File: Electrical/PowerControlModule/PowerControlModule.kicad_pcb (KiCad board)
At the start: 4 copper layers, 47 parts, among them J1 178.6164.0002, J10 Screw_Terminal_01x02, J11 Screw_Terminal_01x02, J12 Screw_Terminal_01x02, J13 Screw_Terminal_01x02, J14 Screw_Terminal_01x02, J15 Screw_Terminal_01x02, J16 Screw_Terminal_01x02, J17 Conn_01x03, J2 178.6164.0002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

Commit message: Fixes silkscreen stuff and adds ground connection for motor control battery connection
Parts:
- renumbered J17 to PowerConnection1
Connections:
- CONN10 pad 2: Net-(CONN10-Pad2) -> GND
- CONN11 pad 2: Net-(CONN11-Pad2) -> GND
- CONN12 pad 2: Net-(CONN11-Pad2) -> GND
- CONN9 pad 2: Net-(CONN10-Pad2) -> GND
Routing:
- net GND: track 0.00 -> 56.8 mm
- net Net-(CONN11-Pad2): track 28.9 -> 0.00 mm
- net Net-(CONN10-Pad2): track 27.9 -> 0.00 mm
- net +12V: track 6.88 -> 0.00 mm
- added copper zone on In1.Cu, net +12V
- added copper zone on In2.Cu, net GND
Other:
- net class Power: clearance 1 -> 0.5
- board text added: "+"
- board text added: "-"
- board text added: "12V"
- board text added: "ENABLE"
- board text added: "GND"

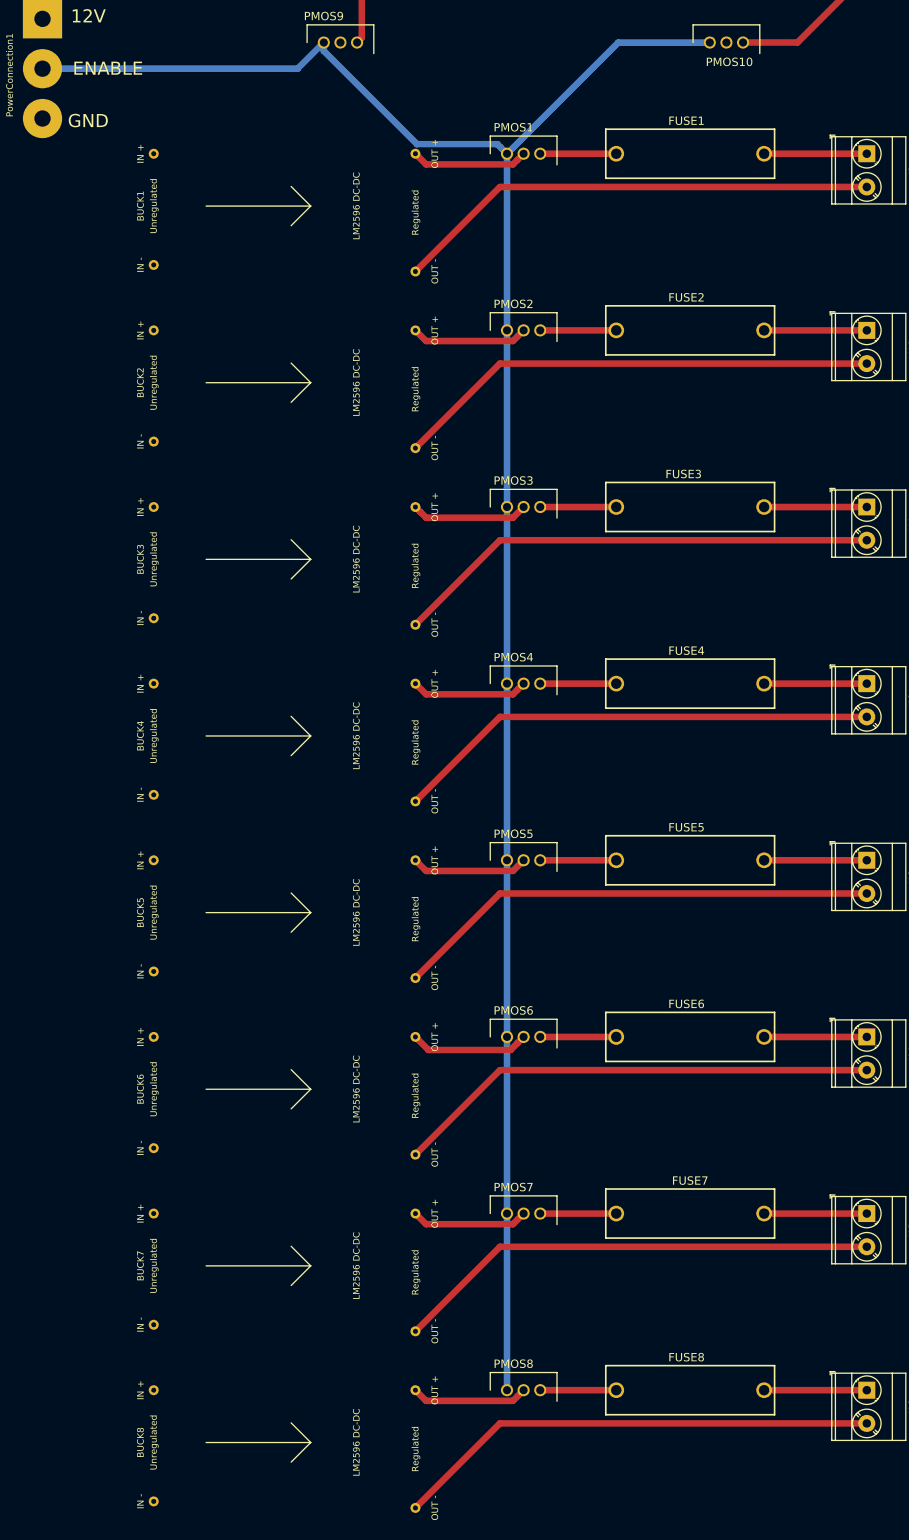
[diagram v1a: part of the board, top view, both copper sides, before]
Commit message: Rearranges mosfets, fuses and buck converters in correct order. Need to add heatsinks to design and confirm hole sizes. Also need to add safety module eventually
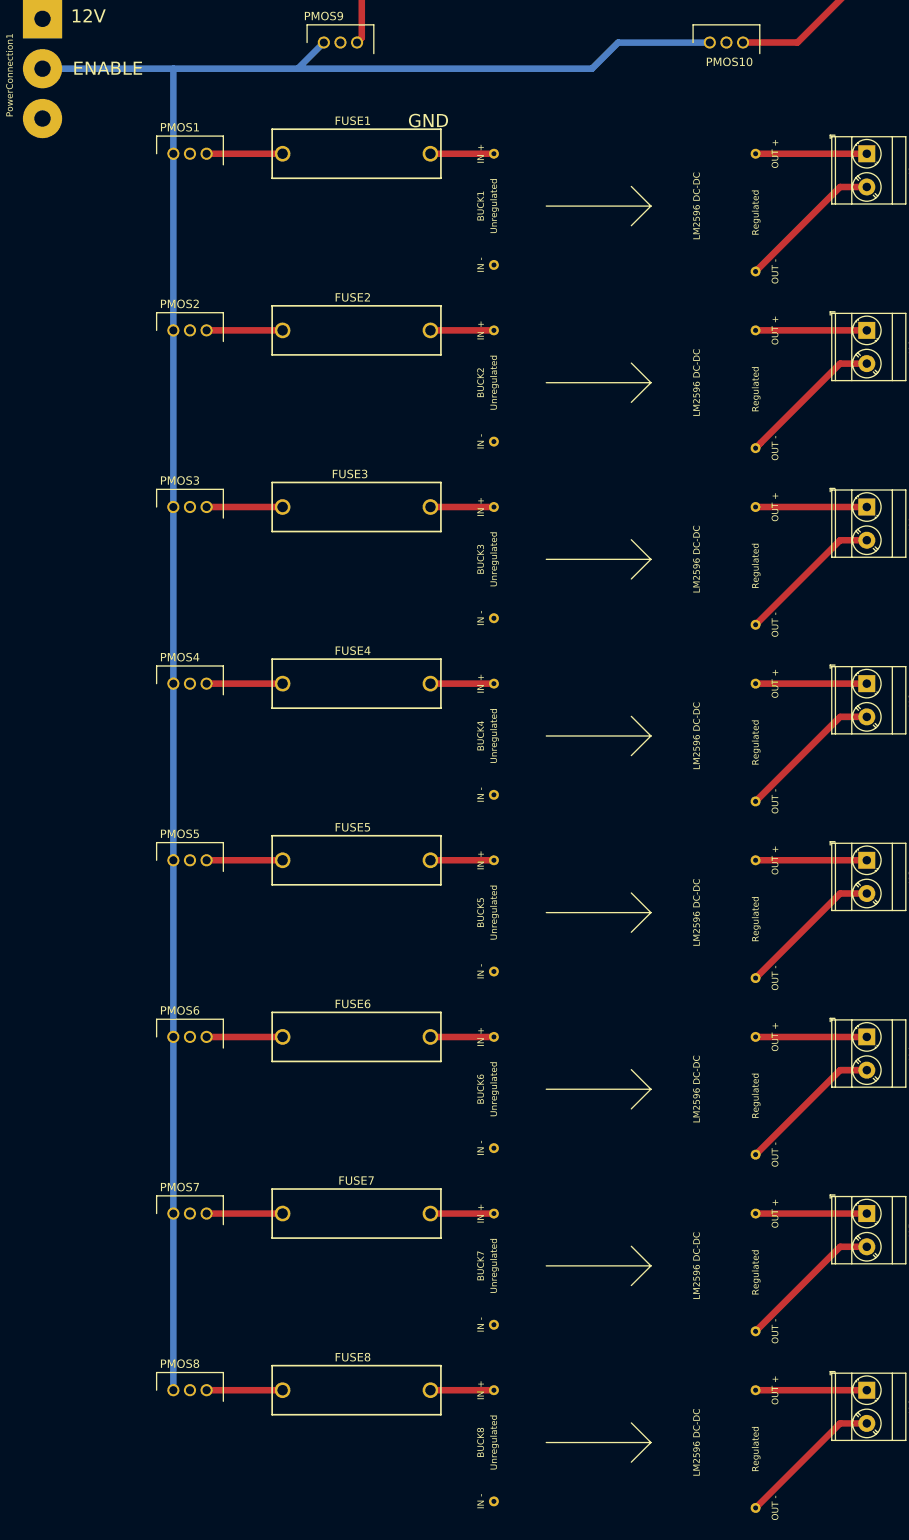
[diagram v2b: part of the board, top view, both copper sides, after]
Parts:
- moved BUCK1 52.0 mm to (368.0, 43.0)
- moved BUCK2 52.0 mm to (368.0, 70.0)
- moved BUCK3 52.0 mm to (368.0, 97.0)
- moved BUCK4 52.0 mm to (368.0, 124.0)
- moved BUCK5 52.0 mm to (368.0, 151.0)
- moved BUCK6 52.0 mm to (368.0, 178.0)
- moved BUCK7 52.0 mm to (368.0, 205.0)
- moved BUCK8 52.0 mm to (368.0, 232.0)
- moved FUSE1 51.0 mm to (350.0, 36.0)
- moved FUSE2 51.0 mm to (350.0, 63.0)
- moved FUSE3 51.0 mm to (350.0, 90.0)
- moved FUSE4 51.0 mm to (350.0, 117.0)
- moved FUSE5 51.0 mm to (350.0, 144.0)
- moved FUSE6 51.0 mm to (350.0, 171.0)
- moved FUSE7 51.0 mm to (350.0, 198.0)
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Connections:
- BUCK1 pad 2: +12V -> Net-(BUCK1-Pad2)
- BUCK2 pad 2: +12V -> Net-(BUCK2-Pad2)
- BUCK3 pad 2: +12V -> Net-(BUCK3-Pad2)
- BUCK4 pad 2: +12V -> Net-(BUCK4-Pad2)
- BUCK5 pad 2: +12V -> Net-(BUCK5-Pad2)
- BUCK6 pad 2: +12V -> Net-(BUCK6-Pad2)
- BUCK7 pad 2: +12V -> Net-(BUCK7-Pad2)
- BUCK8 pad 2: +12V -> Net-(BUCK8-Pad2)
- FUSE1 pad 2: Net-(FUSE1-Pad2) -> Net-(BUCK1-Pad2)
- FUSE2 pad 2: Net-(FUSE2-Pad2) -> Net-(BUCK2-Pad2)
- FUSE3 pad 2: Net-(FUSE3-Pad2) -> Net-(BUCK3-Pad2)
- FUSE4 pad 2: Net-(FUSE4-Pad2) -> Net-(BUCK4-Pad2)
- FUSE5 pad 2: Net-(FUSE5-Pad2) -> Net-(BUCK5-Pad2)
- FUSE6 pad 2: Net-(FUSE6-Pad2) -> Net-(BUCK6-Pad2)
- FUSE7 pad 2: Net-(FUSE7-Pad2) -> Net-(BUCK7-Pad2)
- FUSE8 pad 2: Net-(FUSE8-Pad2) -> Net-(BUCK8-Pad2)
- J10 pad 1: Net-(FUSE2-Pad2) -> Net-(BUCK2-Pad4)
- J11 pad 1: Net-(FUSE3-Pad2) -> Net-(BUCK3-Pad4)
- J12 pad 1: Net-(FUSE4-Pad2) -> Net-(BUCK4-Pad4)
- J13 pad 1: Net-(FUSE5-Pad2) -> Net-(BUCK5-Pad4)
- J14 pad 1: Net-(FUSE6-Pad2) -> Net-(BUCK6-Pad4)
- J15 pad 1: Net-(FUSE7-Pad2) -> Net-(BUCK7-Pad4)
- J16 pad 1: Net-(FUSE8-Pad2) -> Net-(BUCK8-Pad4)
- J9 pad 1: Net-(FUSE1-Pad2) -> Net-(BUCK1-Pad4)
- PMOS1 pad 2: Net-(BUCK1-Pad4) -> +12V
- PMOS2 pad 2: Net-(BUCK2-Pad4) -> +12V
- PMOS3 pad 2: Net-(BUCK3-Pad4) -> +12V
- PMOS4 pad 2: Net-(BUCK4-Pad4) -> +12V
- PMOS5 pad 2: Net-(BUCK5-Pad4) -> +12V
- PMOS6 pad 2: Net-(BUCK6-Pad4) -> +12V
- PMOS7 pad 2: Net-(BUCK7-Pad4) -> +12V
- PMOS8 pad 2: Net-(BUCK8-Pad4) -> +12V
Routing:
- net Net-(BUCK4-Pad3): track 74.4 -> 22.4 mm
- net Net-(BUCK3-Pad3): track 74.4 -> 22.4 mm
- net Net-(BUCK2-Pad3): track 74.4 -> 22.4 mm
- net Net-(BUCK1-Pad3): track 74.4 -> 22.4 mm
- net Net-(BUCK8-Pad3): track 74.4 -> 22.4 mm
- net Net-(BUCK7-Pad3): track 74.4 -> 22.4 mm
- net Net-(BUCK6-Pad3): track 74.4 -> 22.4 mm
- net Net-(BUCK5-Pad3): track 74.4 -> 22.4 mm
- net Net-(FUSE8-Pad2): track 15.7 -> 0.00 mm
- net Net-(FUSE7-Pad2): track 15.7 -> 0.00 mm
- net Net-(FUSE6-Pad2): track 15.7 -> 0.00 mm
- net Net-(FUSE5-Pad2): track 15.7 -> 0.00 mm
- net Net-(FUSE4-Pad2): track 15.7 -> 0.00 mm
- net Net-(FUSE3-Pad2): track 15.7 -> 0.00 mm
- net Net-(FUSE2-Pad2): track 15.7 -> 0.00 mm
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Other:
- net class Power: clearance 0.5 -> 0.25

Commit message: Peripheral changes and rewired PCB
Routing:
- net GND: track 56.8 -> 0.00 mm
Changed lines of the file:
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@@
     (thickness 1.6)
     (drawings 27)
-    (tracks 86)
+    (tracks 84)
     (zones 0)
     (modules 47)
@@
   (layers
     (0 F.Cu signal)
-    (1 In1.Cu power)
+    (1 In1.Cu power hide)
     (2 In2.Cu power)
     (31 B.Cu signal)
@@
   (segment (start 423.92 41.08) (end 411 54) (width 1) (layer F.Cu) (net 17))
   (segment (start 428 41.08) (end 423.92 41.08) (width 1) (layer F.Cu) (net 17))
-  (segment (start 329 -21) (end 356.92 -21) (width 1) (layer F.Cu) (net 18))
-  (segment (start 425 -21) (end 396.08 -21) (width 1) (layer F.Cu) (net 18))
   (segment (start 428 63) (end 411 63) (width 1) (layer F.Cu) (net 19))
   (segment (start 411.761999 80.238001) (end 411 81) (width 1) (layer F.Cu) (net 20))

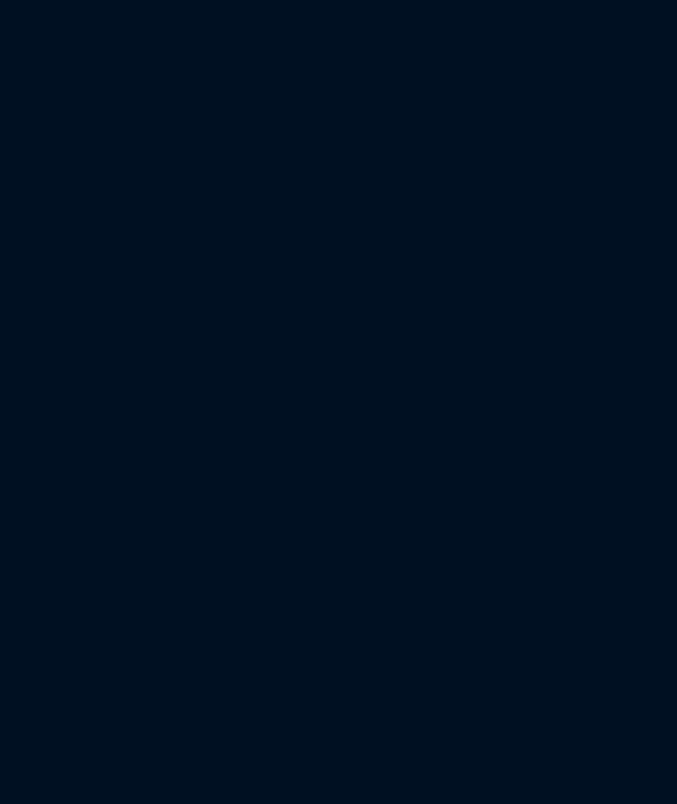
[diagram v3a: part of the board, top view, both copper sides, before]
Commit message: Splits project into multiple modules, peripherals, motors, and safety
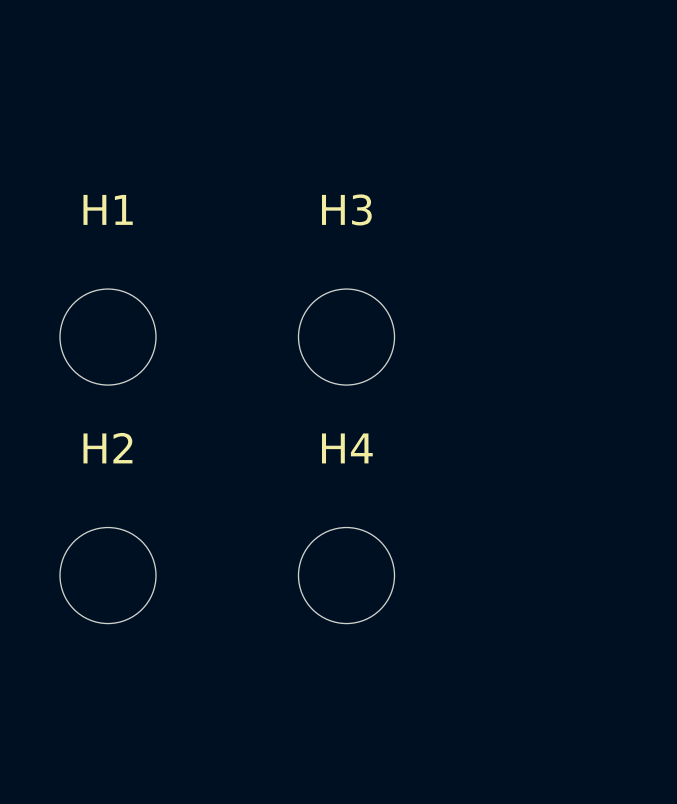
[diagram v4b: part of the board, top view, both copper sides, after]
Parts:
- added H1: MountingHole, MountingHole:MountingHole_3.2mm_M3, F.Cu at (294.0, 164.0)
- added H2: MountingHole, MountingHole:MountingHole_3.2mm_M3, F.Cu at (294.0, 171.9)
- added H3: MountingHole, MountingHole:MountingHole_3.2mm_M3, F.Cu at (301.9, 164.0)
- added H4: MountingHole, MountingHole:MountingHole_3.2mm_M3, F.Cu at (301.9, 171.9)
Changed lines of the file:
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@@
     (tracks 84)
     (zones 0)
-    (modules 47)
+    (modules 51)
     (nets 42)
   )
@@
       (outputformat 1)
       (mirror false)
-      (drillshape 1)
+      (drillshape 0)
       (scaleselection 1)
-      (outputdirectory ""))
+      (outputdirectory "./"))
   )
   (net 0 "")
@@
     (add_net +12V)
     (add_net GND)
+  )
+  (module MountingHole:MountingHole_3.2mm_M3 (layer F.Cu)
+    (at 301.95 171.95)
+    (descr "Mounting Hole 3.2mm, no annular, M3")
+    (tags "mounting hole 3.2mm no annular m3")
+    (attr virtual)
+    (fp_text reference H4 (at 0 -4.2) (layer F.SilkS)
+      (effects (font (size 1 1) (thickness 0.15)))
+    )
+    (fp_text value MountingHole (at 0 4.2) (layer F.Fab)
+      (effects (font (size 1 1) (thickness 0.15)))
+    )
+    (fp_circle (center 0 0) (end 3.45 0) (layer F.CrtYd) (width 0.05))
+    (fp_circle (center 0 0) (end 3.2 0) (layer Cmts.User) (width 0.15))
+    (fp_text user %R (at 0.3 0) (layer F.Fab)
+      (effects (font (size 1 1) (thickness 0.15)))
+    )
+    (pad 1 np_thru_hole circle (at 0 0) (size 3.2 3.2) (drill 3.2) (layers *.Cu *.Mask))
+  )
+  (module MountingHole:MountingHole_3.2mm_M3 (layer F.Cu)
+    (at 301.95 164)
+    (descr "Mounting Hole 3.2mm, no annular, M3")
+    (tags "mounting hole 3.2mm no annular m3")
+    (attr virtual)
+    (fp_text reference H3 (at 0 -4.2) (layer F.SilkS)
+      (effects (font (size 1 1) (thickness 0.15)))
+    )
+    (fp_text value MountingHole (at 0 4.2) (layer F.Fab)
+      (effects (font (size 1 1) (thickness 0.15)))
+    )
+    (fp_circle (center 0 0) (end 3.45 0) (layer F.CrtYd) (width 0.05))
+    (fp_circle (center 0 0) (end 3.2 0) (layer Cmts.User) (width 0.15))
+    (fp_text user %R (at 0.3 0) (layer F.Fab)
+      (effects (font (size 1 1) (thickness 0.15)))
+    )
+    (pad 1 np_thru_hole circle (at 0 0) (size 3.2 3.2) (drill 3.2) (layers *.Cu *.Mask))
+  )
+  (module MountingHole:MountingHole_3.2mm_M3 (layer F.Cu)
+    (at 294 171.95)
+    (descr "Mounting Hole 3.2mm, no annular, M3")
+    (tags "mounting hole 3.2mm no annular m3")
+    (attr virtual)
+    (fp_text reference H2 (at 0 -4.2) (layer F.SilkS)
+      (effects (font (size 1 1) (thickness 0.15)))
+    )
+    (fp_text value MountingHole (at 0 4.2) (layer F.Fab)
+      (effects (font (size 1 1) (thickness 0.15)))
+    )
+    (fp_circle (center 0 0) (end 3.45 0) (layer F.CrtYd) (width 0.05))
+    (fp_circle (center 0 0) (end 3.2 0) (layer Cmts.User) (width 0.15))
+    (fp_text user %R (at 0.3 0) (layer F.Fab)
+      (effects (font (size 1 1) (thickness 0.15)))
+    )
+    (pad 1 np_thru_hole circle (at 0 0) (size 3.2 3.2) (drill 3.2) (layers *.Cu *.Mask))
+  )
+  (module MountingHole:MountingHole_3.2mm_M3 (layer F.Cu)
+    (at 294 164)
+    (descr "Mounting Hole 3.2mm, no annular, M3")
+    (tags "mounting hole 3.2mm no annular m3")
+    (attr virtual)
+    (fp_text reference H1 (at 0 -4.2) (layer F.SilkS)
+      (effects (font (size 1 1) (thickness 0.15)))
+    )
+    (fp_text value MountingHole (at 0 4.2) (layer F.Fab)
+      (effects (font (size 1 1) (thickness 0.15)))
+    )
+    (fp_circle (center 0 0) (end 3.45 0) (layer F.CrtYd) (width 0.05))
+    (fp_circle (center 0 0) (end 3.2 0) (layer Cmts.User) (width 0.15))
+    (fp_text user %R (at 0.3 0) (layer F.Fab)
+      (effects (font (size 1 1) (thickness 0.15)))
+    )
+    (pad 1 np_thru_hole circle (at 0 0) (size 3.2 3.2) (drill 3.2) (layers *.Cu *.Mask))
   )
   (module SCR_KiCAD_Lib:LM2596 (layer F.Cu)
@@
     (polygon
       (pts
-        (xy 293 -28) (xy 292 252) (xy 442 252) (xy 442 -28)
+        (xy 287.75 -30) (xy 286 254) (xy 452 254.001599) (xy 452.25 -30)
       )
     )
